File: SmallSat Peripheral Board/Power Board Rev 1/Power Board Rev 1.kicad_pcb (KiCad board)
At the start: 2 copper layers, 41 parts, among them J1 Conn_01x02_Pin, J2 Conn_01x02_Pin, U1 DMN3020UFDF, U2 BQ296202DSGR, U3 DMN3020UFDF, U4 BQ28Z620DRZR, U5 TPS62993QRYTRQ1, U6 TPS62993QRYTRQ1

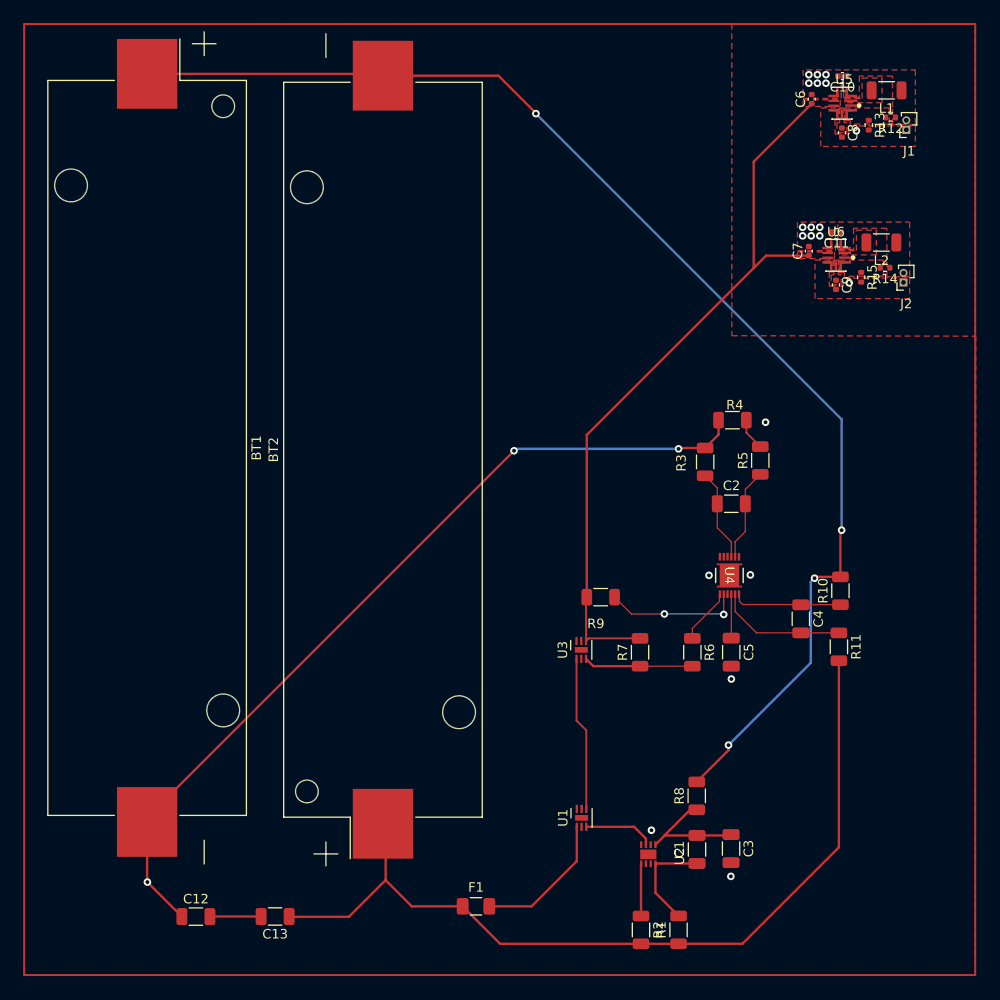
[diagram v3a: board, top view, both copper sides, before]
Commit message: Power Board Rev 1 Gerber Files Generated
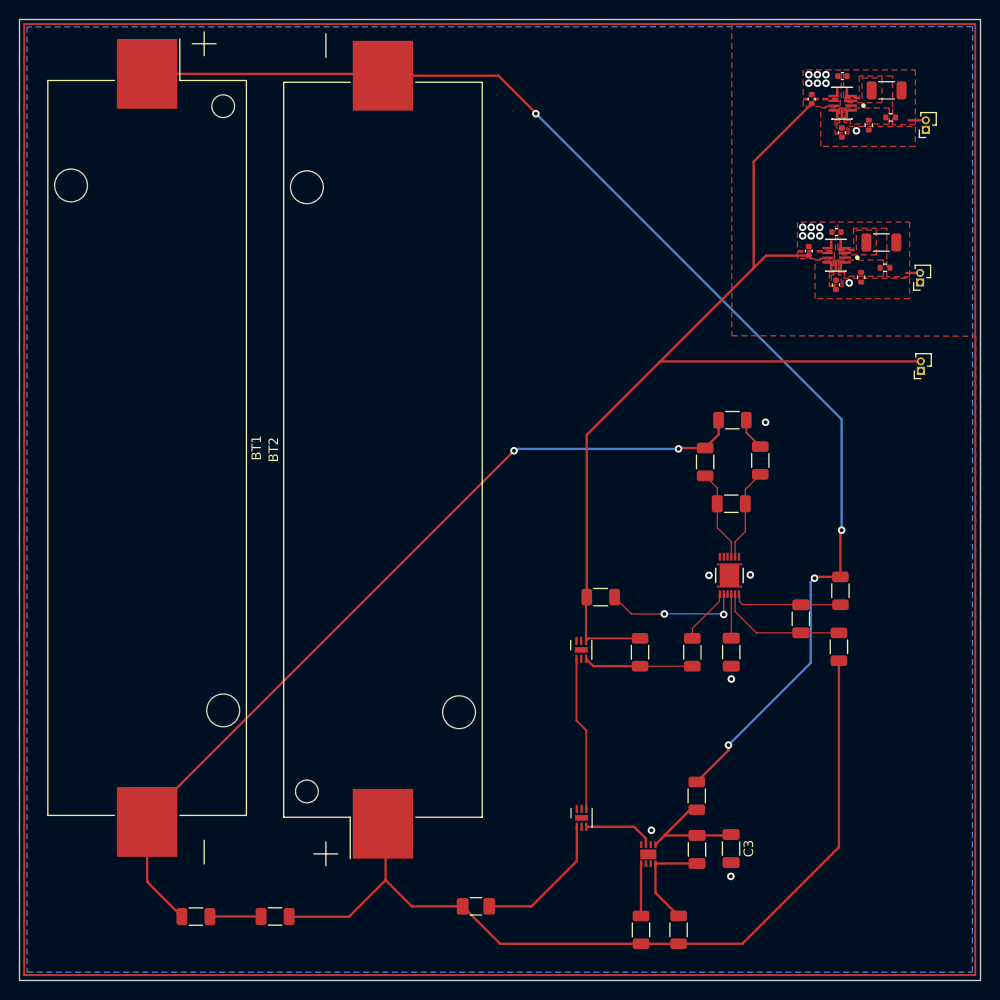
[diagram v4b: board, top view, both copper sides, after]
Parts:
- added J3: Conn_01x02_Pin, Connector_PinSocket_1.00mm:PinSocket_1x02_P1.00mm_Vertical, F.Cu at (171.3, 94.0)
- moved J1 2.05 mm to (171.8, 68.6)
- moved J2 1.75 mm to (171.2, 84.7)
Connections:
- C12 pad 1: GND -> /BATT-
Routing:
- net /PACK+: track 78.6 -> 106.1 mm
- net GND: track 18.0 -> 3.39 mm, vias 21 -> 20
- net /BATT-: track 78.5 -> 90.0 mm
- net /3.3V: track 0.00 -> 1.85 mm
- net /5V: track 0.00 -> 1.45 mm
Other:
- board outline added: 101.1 x 101.1 mm

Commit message: PB-order version
Sent the order in for Rev 1 power board with this version
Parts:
- added J4: Conn_01x02_Pin, Connector_PinSocket_1.00mm:PinSocket_1x02_P1.00mm_Vertical, F.Cu at (142.8, 110.3)
- L1, L2: footprint Inductor_SMD:L_1206_3216Metric -> Inductor_SMD:L_1210_3225Metric
- moved L1 0.55 mm to (167.9, 64.0)
- moved L2 0.48 mm to (167.3, 80.0)
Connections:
- net /FB_VSET_3V3 renamed /V_Regulation/FB_VSET_3V3
- net /FB_VSET_5V renamed /V_Regulation/FB_VSET_5V
- net /SS_TR_3V3 renamed /V_Regulation/SS_TR_3V3
- net /SS_TR_5V renamed /V_Regulation/SS_TR_5V
- net /SW_3V3 renamed /V_Regulation/SW_3V3
- net /SW_5V renamed /V_Regulation/SW_5V
- U4 pad 5: /FUEL_SCL -> /Fuel_SCL
- U4 pad 6: /FUEL_SDA -> /Fuel_SDA
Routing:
- net /Fuel_SCL: track 0.00 -> 9.05 mm
- net /Fuel_SDA: track 0.00 -> 8.20 mm
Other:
- board text added: "3.3V"
- board text added: "5V"
- board text added: "7.4V"
